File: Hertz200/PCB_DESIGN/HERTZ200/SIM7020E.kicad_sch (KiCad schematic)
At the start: 23 parts

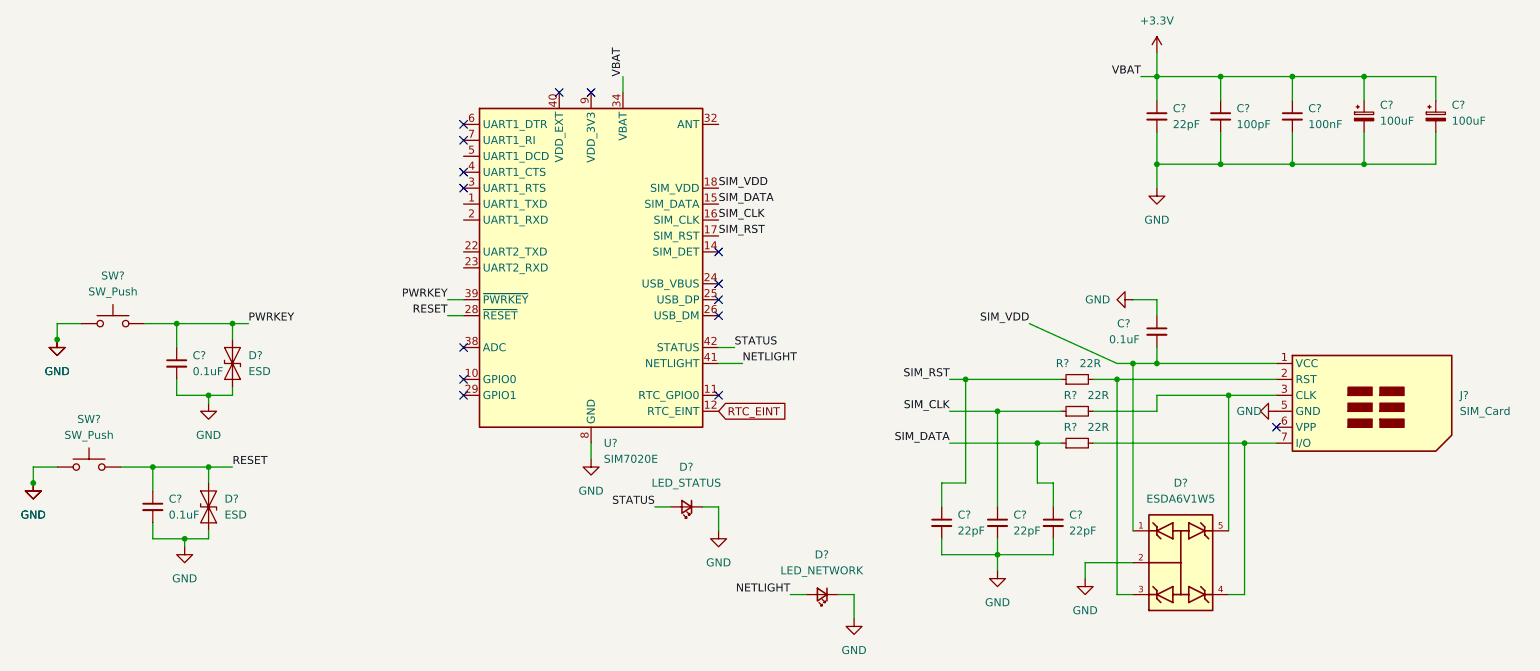
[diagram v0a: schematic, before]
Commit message: SIMCARD-POWER-SECTION
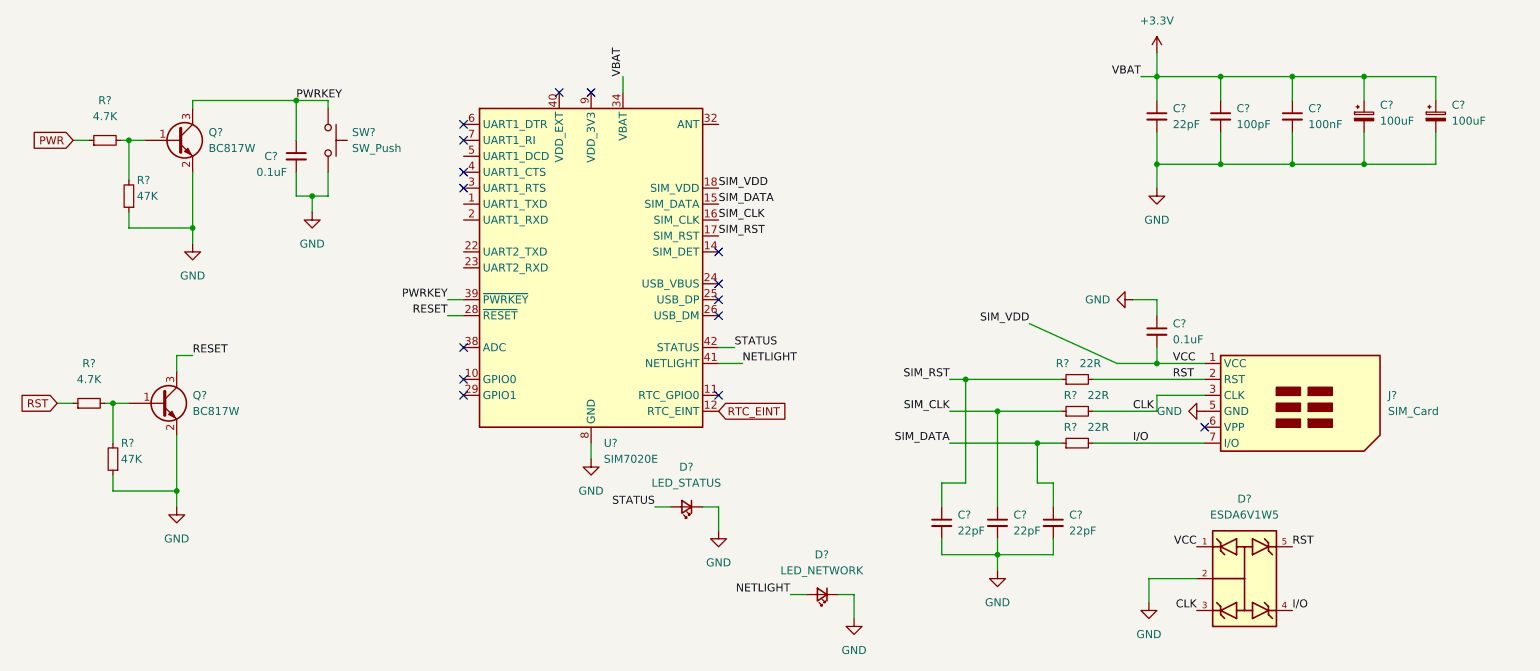
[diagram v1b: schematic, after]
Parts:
- removed C? (x2): 0.1uF, symbol Device:C_Small
- removed D? (x2): ESD, Diode_SMD:D_SOD-923, symbol Diode:ESD9B3.3ST5G
- removed SW? (x2): SW_Push, symbol Switch:SW_Push
- added C?: 0.1uF, symbol Device:C_Small
- added Q? (x2): BC817W, Package_TO_SOT_SMD:SOT-323_SC-70, symbol Transistor_BJT:BC817W
- added R? (x2): 4.7K, symbol Device:R_Small
- added R? (x2): 47K, symbol Device:R_Small
- added SW?: SW_Push, symbol Switch:SW_Push
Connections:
- net GND: now also C?.2, Q?.2 (E), Q?.2 (E), R?.1, R?.1, SW?.2
- net PWRKEY: now also C?.1, Q?.3 (C), SW?.1
- net RESET: now also Q?.3 (C)
- net RST: now reaches J?.2 (RST), R?.2
- net RST: now also D?.5, R?.1; no longer D?.3
- net I/O: now reaches D?.4, J?.7 (I/O), R?.2
- net CLK: now reaches J?.3 (CLK), R?.2
- net CLK: now also D?.3; no longer D?.5
- new net: Q?.1 (B), R?.2, R?.2 (x2)
- new net PWR: R?.1
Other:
- moved on the sheet: D?, J?
